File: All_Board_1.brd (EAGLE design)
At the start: 52 x 69.4 mm, 71 parts, among them J1 61301611121, J2 61301611121, T10 BC817U, T11 BC817U, T12 BC817U, T13 BC817U, T14 BC817U, T7 BC817U, T8 BC817U, T9 BC817U

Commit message: pierwsza docelowa wersja
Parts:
- added C1, C4: 100nF, rcl:C0805K
- added C2, C5: 10uF, rcl:C0805K
- added G1: (no value), infineon:SOT230P700X170-4N-1
- added J3, J4: 61301611121, Headers:61301611121
- added J5: 62000311121, Headers:62000311121
- added J7: 62000811121, Headers:62000811121
- added JP4: (no value), pinhead:2X02
- added JP5: (no value), pinhead:2X04
- added R53, R56, R59, R60, R64, R65, R66, R67, R68, R69, R70, R71: 10K, rcl:R0805
- added R57, R61, R62, R63: 4,7K, rcl:R0805
- added R58: 47K, rcl:R0805
- added S1: (no value), switch-dil:DIP02YL
- added T1, T2, T3: BC817U, transistor:INF-SC74
- added U$1: USB-SERIAL-CH340, diy-modules:USB-SERIAL-CH340
- added U$4: WIRELESS-WIFI-ESP-01, diy-modules:WIRELESS-WIFI-ESP-01
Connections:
- new net +3V1: C4.1, C5.1, G1.2, G1.4, J4.5, J4.6, J7.8, JP4.1, JP4.2, JP4.3, JP4.4, R57.1, R58.2, R59.1, R60.1, R61.1, R62.1, R63.1, R64.2, R65.2, R66.2, R67.2, U$4.D2
- new net +5V1: C1.1, C2.1, G1.3, J4.15, J4.16, R68.2, R69.2, R70.2, R71.2, U$1.PLUS
- new net D+1: J3.13, U$1.D+
- new net D-1: J3.14, U$1.D-
- new net DTR: J7.1, R53.1, T1.4, U$1.DTR
- new net ENABLE1: R60.2, U$4.C2
- new net GND1: C1.2, C2.2, C4.2, C5.2, G1.1, J4.7, J4.8, J7.7, U$1.GND, U$1.MINUS, U$4.A1
- new net GPIO17: J4.9, J7.4, R64.1, T1.3, T2.1, U$4.C1
- new net GPIO18: R66.1, T3.1, U$4.B1
- new net GPIO19: R65.1, S1.2, T2.4
- new net GPIO20: R67.1, S1.1, T3.4
- new net LL10: JP5.3, JP5.4, R69.1, T2.3
- new net LL9: JP5.1, JP5.2, R68.1, T2.6
- new net N$10: J5.1, U$1.5V
- new net N$11: J5.2, U$1.VCC
- new net N$13: J5.3, U$1.3V3
- new net N$17: R63.2, T2.2
- new net N$18: R62.2, T2.5
- new net N$19: R61.2, T3.2
- new net N$21: R57.2, T3.5
- new net N$5: R56.1, T1.5
- new net N$9: R53.2, T1.2
- new net RESET1: J4.10, J4.14, J7.3, R59.2, T1.6, U$4.B2
- new net RTS: J7.2, R56.2, T1.1, U$1.RTS
- new net RXD1: J4.4, J7.5, S1.3, U$1.RXD, U$4.A2
- new net SCL1: JP5.7, JP5.8, R71.1, T3.3
- new net SDA1: JP5.5, JP5.6, R70.1, T3.6
- new net TXD1: J4.3, J7.6, R58.1, S1.4, U$1.TXD, U$4.D1
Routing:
- net +3V1: track 0.00 -> 214.4 mm, vias 0 -> 6
- net GND1: track 0.00 -> 152.4 mm, vias 0 -> 6
- net +5V1: track 0.00 -> 136.6 mm, vias 0 -> 4
- net GPIO17: track 0.00 -> 131.7 mm, vias 0 -> 4
- net TXD1: track 0.00 -> 86.0 mm, vias 0 -> 4
- net RXD1: track 0.00 -> 80.3 mm, vias 0 -> 4
- net DTR: track 0.00 -> 53.9 mm, vias 0 -> 4
- net RESET1: track 0.00 -> 48.9 mm, vias 0 -> 4
- net GPIO20: track 0.00 -> 47.8 mm, vias 0 -> 2
- net RTS: track 0.00 -> 45.6 mm, vias 0 -> 2
- net GPIO19: track 0.00 -> 41.6 mm
- net GPIO18: track 0.00 -> 25.9 mm, vias 0 -> 2
- net LL10: track 0.00 -> 19.3 mm, vias 0 -> 2
- net D+1: track 0.00 -> 19.2 mm
- net D-1: track 0.00 -> 18.9 mm
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- added copper zone on layer 16, net GND1
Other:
- board size 52 x 69.4 mm -> 110 x 69.4 mm
- board text added: "3,3V"
- board text added: "5V"
- board text added: "ANTENNA"
- board text added: "DTR"
- board text added: "ESP-01"
- board text added: "GND"
- board text added: "GPIO - ON"
- board text added: "RTS"
- board text added: "RX"
- board text added: "TX"
- board text added: "USB - UART"
- board text added: "VCC"

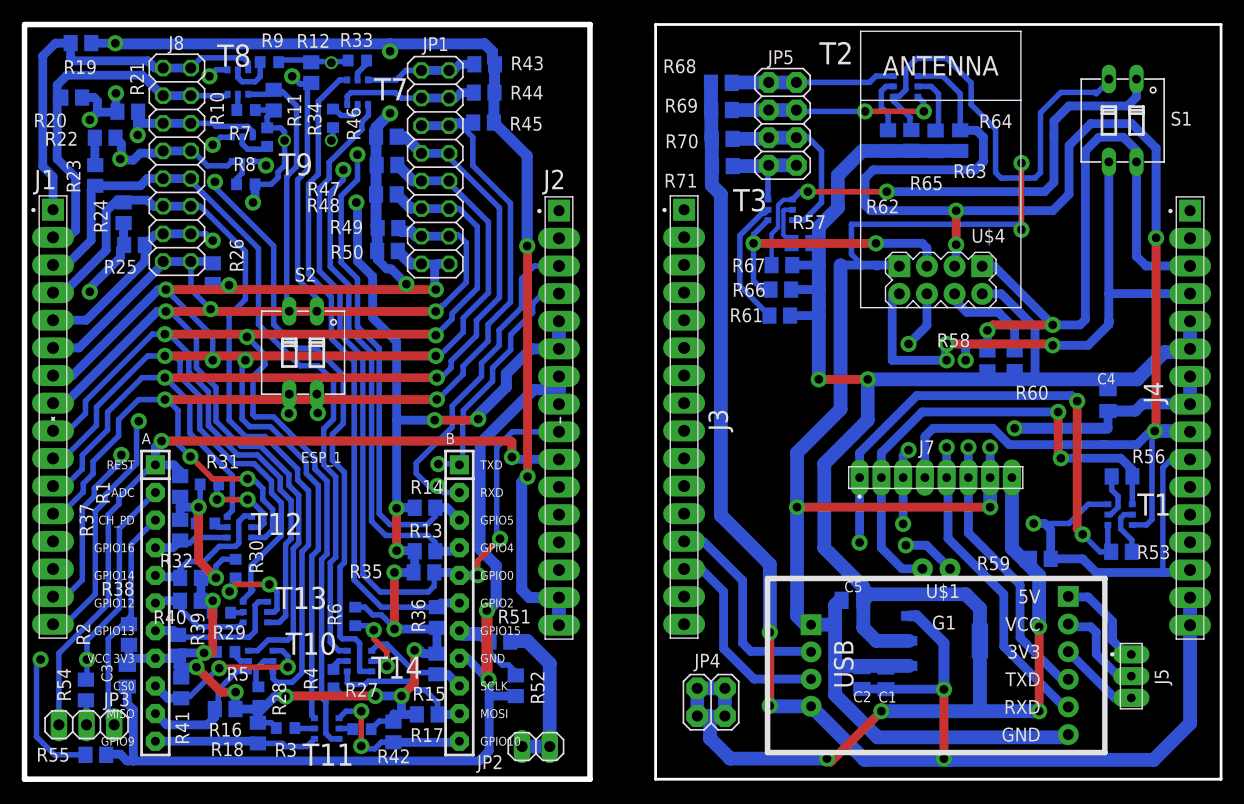
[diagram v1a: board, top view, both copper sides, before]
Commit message: powiekszonyy odstepy miedzy sciezkami
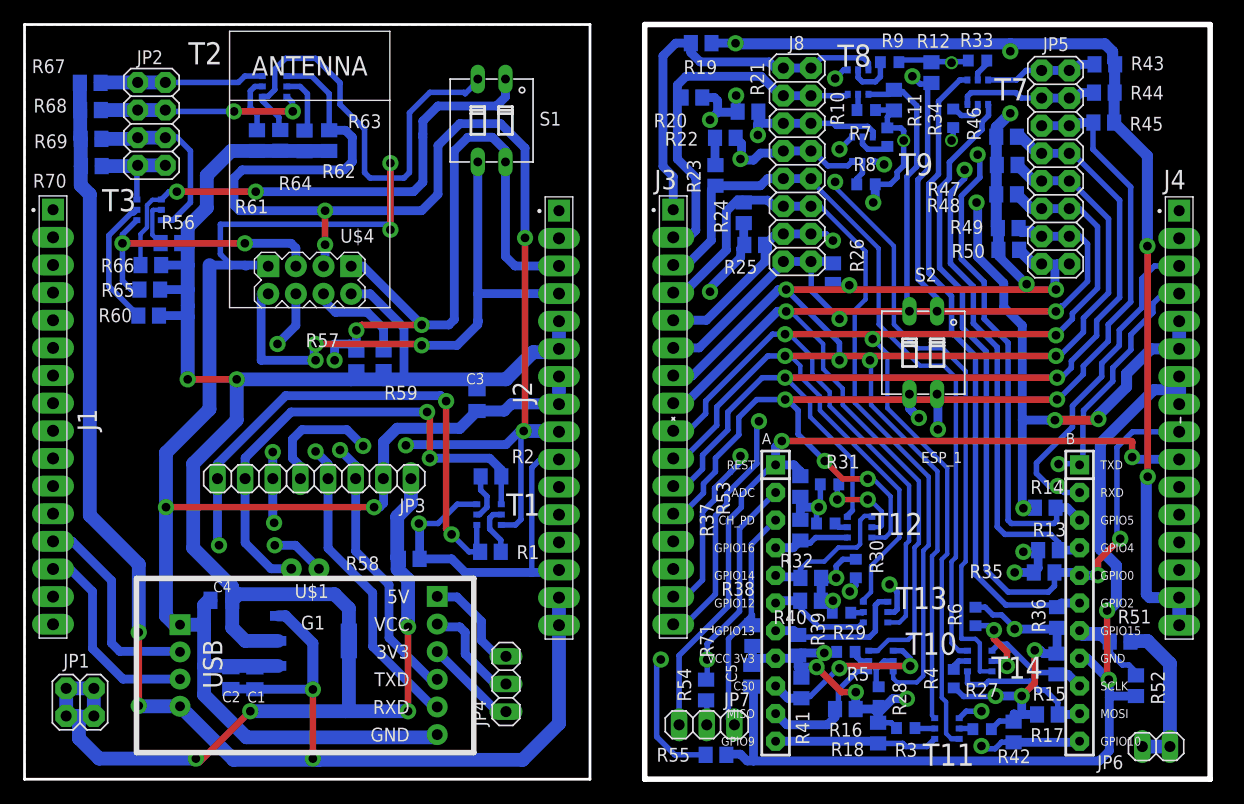
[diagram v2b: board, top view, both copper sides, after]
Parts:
- removed J5: 62000311121, Headers:62000311121
- removed J7: 62000811121, Headers:62000811121
- added JP6: (no value), pinhead:1X02
- added JP7: (no value), pinhead:1X03
- C4: value 100nF -> 10uF
- C5: value 10uF -> 100nF
- JP1: device pinhead:2X08 -> pinhead:2X02
- JP2: device pinhead:1X02 -> pinhead:2X04
- JP3: device pinhead:1X03 -> pinhead:1X08
- JP4: device pinhead:2X02 -> pinhead:1X03
- JP5: device pinhead:2X04 -> pinhead:2X08
- R56, R60: value 10K -> 4,7K
- R57: value 4,7K -> 47K
- R58: value 47K -> 10K
- R63: value 4,7K -> 10K
- moved R56 90.0 mm to (13.4, 49.3), turned to 0 degrees
- moved C4 83.5 mm to (18.1, 16.4), turned to 0 degrees
- moved R60 79.7 mm to (11.4, 42.6), turned to 0 degrees
- moved R65 71.3 mm to (11.5, 45.0), turned to 180 degrees
- moved JP2 67.3 mm to (11.7, 60.2), turned to 270 degrees
- moved R67 65.7 mm to (6.04, 64.0), turned to 0 degrees
- moved R59 63.0 mm to (33.0, 38.5), turned to 90 degrees
- moved R64 62.5 mm to (23.5, 58.7)
- moved JP1 59.0 mm to (5.10, 7.08), turned to 0 degrees
- moved R68 58.0 mm to (6.07, 61.5)
- moved R70 58.0 mm to (6.14, 56.4)
- moved R69 58.0 mm to (6.12, 58.9)
- moved S1 58.0 mm to (42.9, 60.5)
- moved U$1 58.0 mm to (25.8, 10.4)
- moved C1 58.0 mm to (21.2, 9.27)
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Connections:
- net +3V1: now also ESP_1.8, R10.1, R11.2, R12.2, R13.2, R14.2, R15.2, R16.2, R17.2, R18.2, R27.1, R28.1, R29.1, R3.1, R30.1, R31.1, R32.1, R33.1, R34.1, R35.2, R36.2, R37.2, R38.2, R39.2, R4.1, R40.2, R41.2, R42.2, R5.1, R53.1, R6.1, R7.1, R71.1, R8.1, R9.1; no longer C4.1, G1.2, G1.4, J7.8, JP4.1, JP4.2, JP4.3, JP4.4, R57.1, R58.2, R59.1, R60.1, R61.1, R62.1, R63.1, R64.2, R65.2, R66.2, R67.2, U$4.D2
- net +3V3: now also C4.1, G1.2, G1.4, JP1.1, JP1.2, JP1.3, JP1.4, JP3.1, R56.1, R57.2, R58.1, R59.1, R60.1, R61.1, R62.1, R63.2, R64.2, R65.2, R66.2, U$4.D2; no longer ESP_1.8, R1.1, R10.1, R11.2, R12.2, R13.2, R14.2, R15.2, R16.2, R17.2, R18.2, R2.1, R27.1, R28.1, R29.1, R3.1, R30.1, R31.1, R32.1, R33.1, R34.1, R35.2, R36.2, R37.2, R38.2, R39.2, R4.1, R40.2, R41.2, R42.2, R5.1, R6.1, R7.1, R8.1, R9.1
- net +5V: now also C1.1, C2.1, G1.3, R67.2, R68.2, R69.2, R70.2, U$1.PLUS; no longer R19.2, R20.2, R21.2, R22.2, R23.2, R24.2, R25.2, R26.2, R43.2, R44.2, R45.2, R46.2, R47.2, R48.2, R49.2, R50.2
- net +5V1: now also R19.2, R20.2, R21.2, R22.2, R23.2, R24.2, R25.2, R26.2, R43.2, R44.2, R45.2, R46.2, R47.2, R48.2, R49.2, R50.2; no longer C1.1, C2.1, G1.3, R68.2, R69.2, R70.2, R71.2, U$1.PLUS
- net D+: now also U$1.D+
- net D+1: no longer U$1.D+
- net D-: now also U$1.D-
- net D-1: no longer U$1.D-
- net DTR: now also JP3.8, R1.1; no longer J7.1, R53.1
- net ENABLE: now also R59.2, U$4.C2; no longer ESP_1.3, JP3.1, R2.2
- net ENABLE1: now also ESP_1.3, JP7.1, R71.2; no longer R60.2, U$4.C2
- net GND: now also C1.2, C2.2, C4.2, G1.1, JP3.2, U$1.GND, U$1.MINUS, U$4.A1; no longer ESP_1.16, R52.1, R55.1
- net GND1: now also ESP_1.16, R52.1, R55.1; no longer C1.2, C2.2, C4.2, G1.1, J7.7, U$1.GND, U$1.MINUS, U$4.A1
- net GPIO0: now also JP3.5, R63.1, T1.3, T2.1, U$4.C1; no longer ESP_1.13, R35.1, T7.1
- net GPIO1: now also R64.1, S1.2, T2.4; no longer R11.1, S2.2, T8.1
- net GPIO10: now also ESP_1.20, R15.1, T14.1; no longer ESP_1.22, R42.1, T11.1
- net GPIO15: now also JP6.1, JP6.2; no longer JP2.1, JP2.2
- net GPIO17: now also ESP_1.21, R17.1, T14.4; no longer J4.9, J7.4, R64.1, T1.3, T2.1, U$4.C1
- net GPIO18: now also ESP_1.22, R42.1, T11.1; no longer R66.1, T3.1, U$4.B1
- net GPIO19: now also R11.1, S2.2, T8.1; no longer R65.1, S1.2, T2.4
- net GPIO2: now also R65.1, T3.1, U$4.B1; no longer ESP_1.14, R36.1, T7.4
- net GPIO20: now also R12.1, S2.1, T8.4; no longer R67.1, S1.1, T3.4
- net GPIO3: now also R66.1, S1.1, T3.4; no longer R12.1, S2.1, T8.4
- net GPIO4: now also ESP_1.13, J4.9, R35.1, T7.1; no longer ESP_1.12, R13.1, T9.1
- net GPIO6: now also ESP_1.12, R13.1, T9.1; no longer ESP_1.20, R15.1, T14.1
- net GPIO8: now also ESP_1.14, R36.1, T7.4; no longer ESP_1.21, R17.1, T14.4
- net LED_A1: now also J3.9, JP5.11, JP5.12; no longer J1.9, JP1.11, JP1.12
- net LED_A2: now also J3.10, JP5.10, JP5.9; no longer J1.10, JP1.10, JP1.9
- net LED_A3: now also J3.11, JP5.7, JP5.8; no longer J1.11, JP1.7, JP1.8
- net LED_A4: now also J3.12, JP5.5, JP5.6; no longer J1.12, JP1.5, JP1.6
- net LL1: now also JP2.1, JP2.2, R67.1, T2.6; no longer J1.1, J8.1, J8.2, R19.1, T8.6
- net LL10: now also J3.8, JP5.13, JP5.14, R49.1, T10.6; no longer JP5.3, JP5.4, R69.1, T2.3
- net LL2: now also JP2.3, JP2.4, R68.1, T2.3; no longer J1.2, J8.3, J8.4, R20.1, T8.3
- net LL3: now also J3.1, J8.1, J8.2, R19.1, T8.6; no longer J1.3, J8.10, J8.9, R23.1, T14.6
- net LL4: now also J3.2, J8.3, J8.4, R20.1, T8.3; no longer J1.4, J8.11, J8.12, R24.1, T10.3
- net LL5: now also J3.3, J8.10, J8.9, R23.1, T14.6; no longer J1.5, J8.13, J8.14, R25.1, T14.3
- net LL6: now also J3.4, J8.11, J8.12, R24.1, T10.3; no longer J1.6, J8.15, J8.16, R26.1, T11.3
- net LL7: now also J3.5, J8.13, J8.14, R25.1, T14.3; no longer J1.7, JP1.15, JP1.16, R50.1, T11.6
- net LL8: now also J3.6, J8.15, J8.16, R26.1, T11.3; no longer J1.8, JP1.13, JP1.14, R49.1, T10.6
- net LL9: now also J3.7, JP5.15, JP5.16, R50.1, T11.6; no longer JP5.1, JP5.2, R68.1, T2.6
- net N$1: now also R2.1, T1.5; no longer JP1.3, JP1.4, R44.1, T7.3
- net N$10: now also JP7.2, R54.2; no longer J5.1, U$1.5V
- net N$11: now also JP4.2; no longer J5.2
- net N$13: now also JP4.1; no longer J5.3
- net N$17: now also R62.2; no longer R63.2
- net N$18: now also R61.2; no longer R62.2
- net N$19: now also R60.2; no longer R61.2
- net N$2: now also R1.2, T1.2; no longer JP3.2, R54.2
- net N$21: now also R56.2; no longer R57.2
- net N$3: now also JP5.1, JP5.2; no longer JP1.1, JP1.2
- net N$5: now also JP4.3, U$1.5V; no longer R56.1, T1.5
- net N$9: now also JP5.3, JP5.4, R44.1, T7.3; no longer R53.2, T1.2
- net RESET: now also JP3.6, R58.2, T1.6, U$4.B2; no longer ESP_1.1, JP3.3, R1.2
- net RESET1: now also ESP_1.1, JP7.3, R53.2; no longer J7.3, R59.2, T1.6, U$4.B2
- net RTS: now also JP3.7, R2.2; no longer J7.2, R56.2
- net RXD: now also JP3.4, S1.3, U$1.RXD, U$4.A2; no longer ESP_1.9, S2.3
- net RXD1: now also ESP_1.9, S2.3; no longer J7.5, S1.3, U$1.RXD, U$4.A2
- net SCL: now also JP2.7, JP2.8, R70.1, T3.3; no longer J1.15, J8.7, J8.8, R22.1, T9.3
- net SCL1: now also J3.15, J8.7, J8.8, R22.1, T9.3; no longer JP5.7, JP5.8, R71.1, T3.3
- net SDA: now also JP2.5, JP2.6, R69.1, T3.6; no longer J1.16, J8.5, J8.6, R21.1, T9.6
- net SDA1: now also J3.16, J8.5, J8.6, R21.1, T9.6; no longer JP5.5, JP5.6, R70.1, T3.6
- net TXD: now also JP3.3, R57.1, S1.4, U$1.TXD, U$4.D1; no longer ESP_1.10, S2.4
- net TXD1: now also ESP_1.10, S2.4; no longer J7.6, R58.1, S1.4, U$1.TXD, U$4.D1
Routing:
- net GPIO17: track 131.7 -> 13.5 mm, vias 4 -> 0
- net LL9: track 15.3 -> 91.5 mm, vias 0 -> 4
- net LL10: track 19.3 -> 93.1 mm
- net GND: track 90.0 -> 154.5 mm, vias 2 -> 4
- net GND1: track 152.4 -> 89.8 mm, vias 6 -> 2
- net +3V1: track 214.4 -> 157.2 mm, vias 6 -> 21
- net RXD: track 25.0 -> 80.0 mm, vias 2 -> 4
- net RXD1: track 80.3 -> 25.8 mm, vias 4 -> 2
- net TXD: track 32.5 -> 85.6 mm, vias 2 -> 4
- net TXD1: track 86.0 -> 34.0 mm, vias 4 -> 2
- net GPIO0: track 78.6 -> 127.9 mm, vias 2 -> 6
- net GPIO8: track 13.5 -> 60.1 mm
- net LL4: track 75.0 -> 33.7 mm
- net GPIO6: track 9.89 -> 45.3 mm, vias 0 -> 2
- net GPIO2: track 60.4 -> 25.9 mm, vias 0 -> 2
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- added copper zone on layer 16, net GND
- removed copper zone on layer 16, net GND1
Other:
- board size 110 x 69.4 mm -> 109 x 69.4 mm
